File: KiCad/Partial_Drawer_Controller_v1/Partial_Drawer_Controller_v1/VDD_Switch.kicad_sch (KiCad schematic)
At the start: 5 parts, among them Q4 AO3400A, Q6 AO3401A

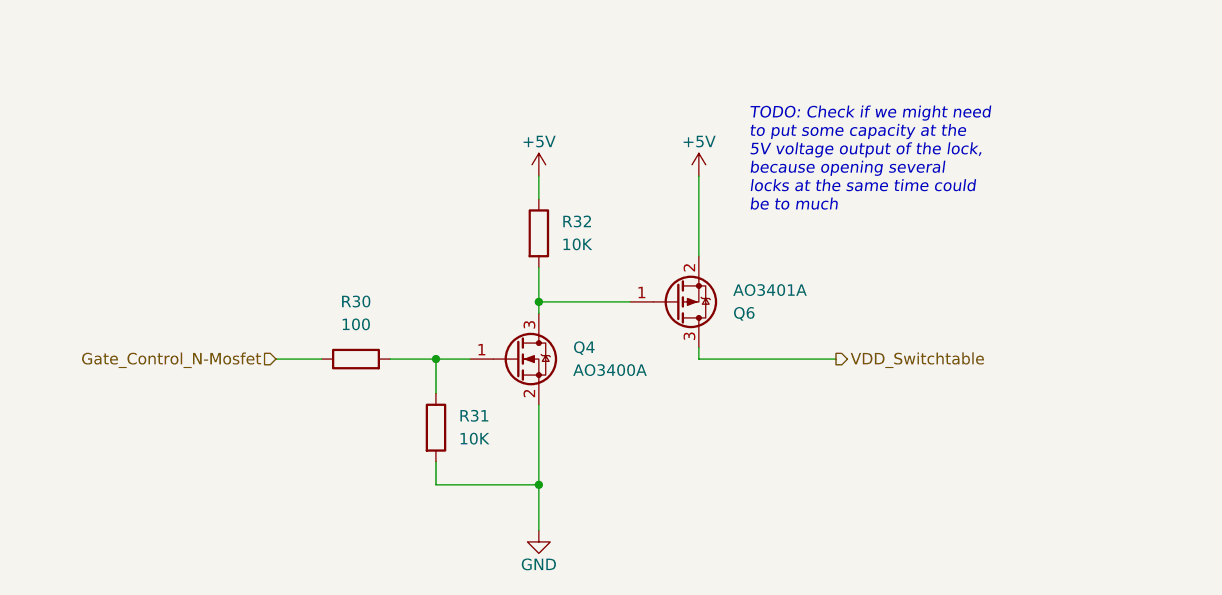
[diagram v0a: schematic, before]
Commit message: feat: started to replace CAN Communication chip to `SN65HVD230` and added todos
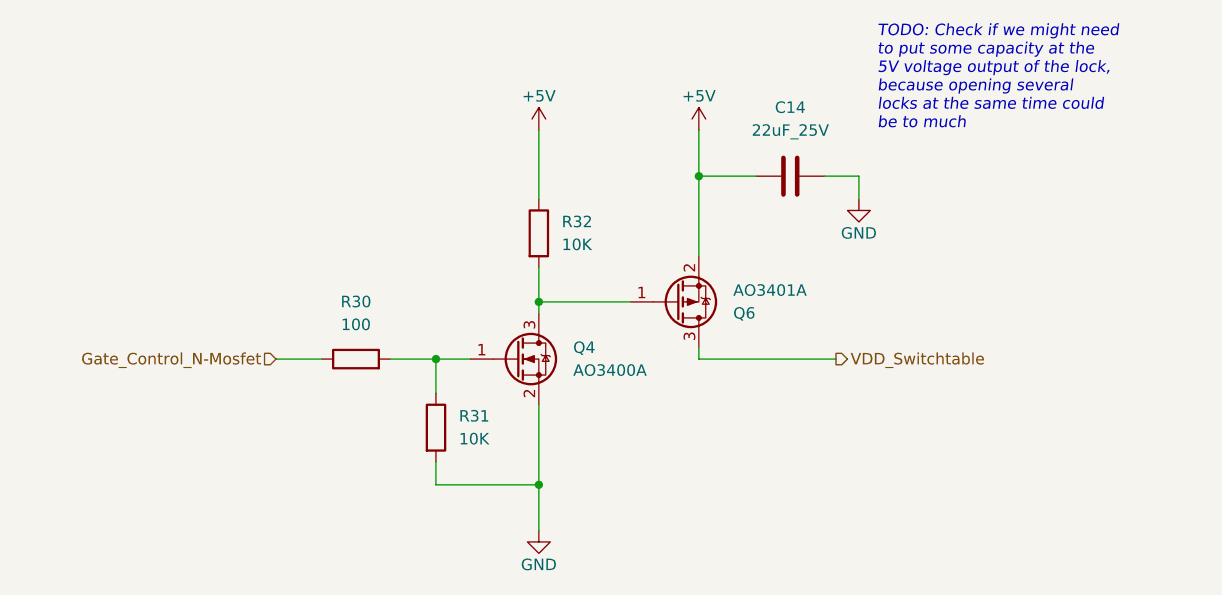
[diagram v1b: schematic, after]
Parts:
- added C14: 22uF_25V, Capacitor_SMD:C_1206_3216Metric, symbol _C_1206:22uF_25V
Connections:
- net +5V: now also C14.1
- net GND: now also C14.2

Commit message: feat: first progress in placing parts
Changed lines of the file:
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@@
-		)
-	)
-	(text_box "TODO: Check if we might need to put some capacity at the 5V voltage output of the lock, because opening several locks at the same time could be to much"
-		(exclude_from_sim no)
-		(at 172.466 46.736 0)
-		(size 31.75 12.7)
-		(stroke
-			(width -0.0001)
-			(type default)
-		)
-		(fill
-			(type none)
-		)
-		(effects
-			(font
-				(size 1.27 1.27)
-				(italic yes)
-				(color 255 0 0 1)
-			)
-			(justify left top)
 		)
 	)

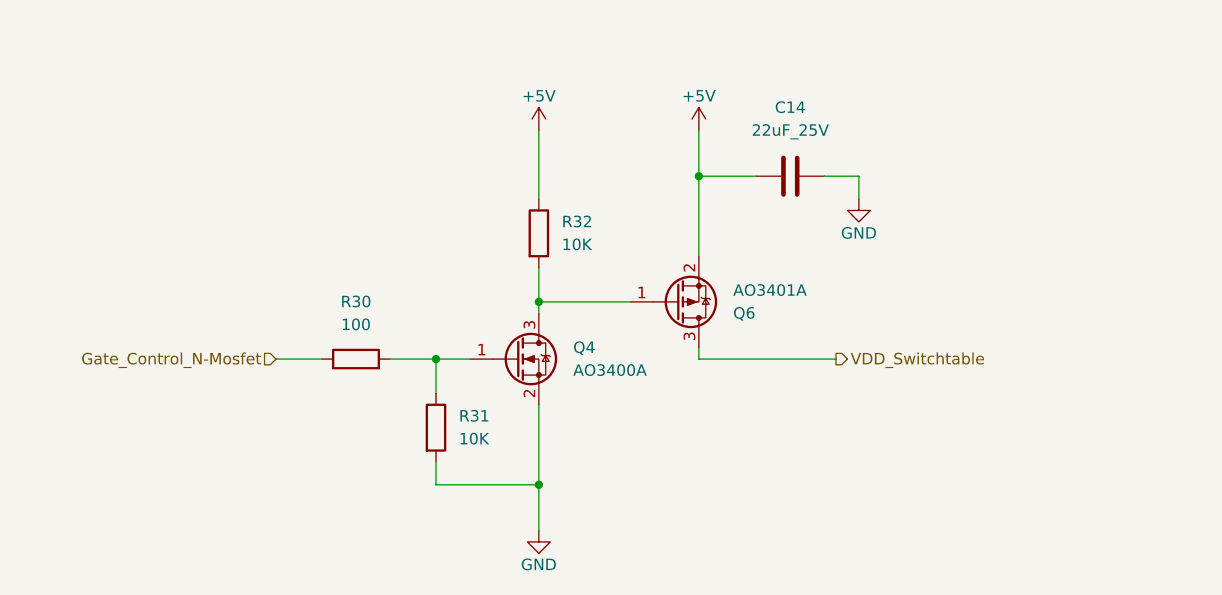
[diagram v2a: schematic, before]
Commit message: feat: minor adjustments and new export of manufacturing files for `Partial_Drawer_controller_v1`
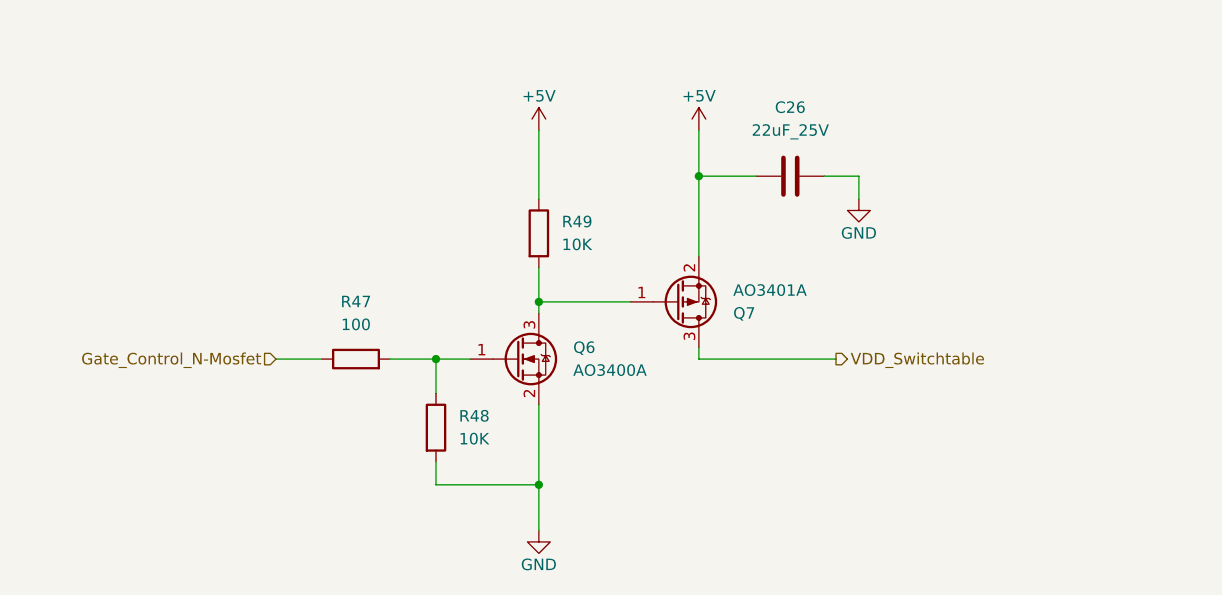
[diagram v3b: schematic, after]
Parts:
- renumbered C14 to C26, Q4 to Q6, Q6 to Q7, R30 to R47, R31 to R48, R32 to R49
